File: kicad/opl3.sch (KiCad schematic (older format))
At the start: 44 parts, among them J1 Conn_01x08, J2 AudioJack2_Ground_Switch, U1 YMF262, U2 YAC512, U3 LM2902, U4 NE5532, U5 74HC595, U6 SN74LVC1G14DBV, X1 ASV-14.318MHz

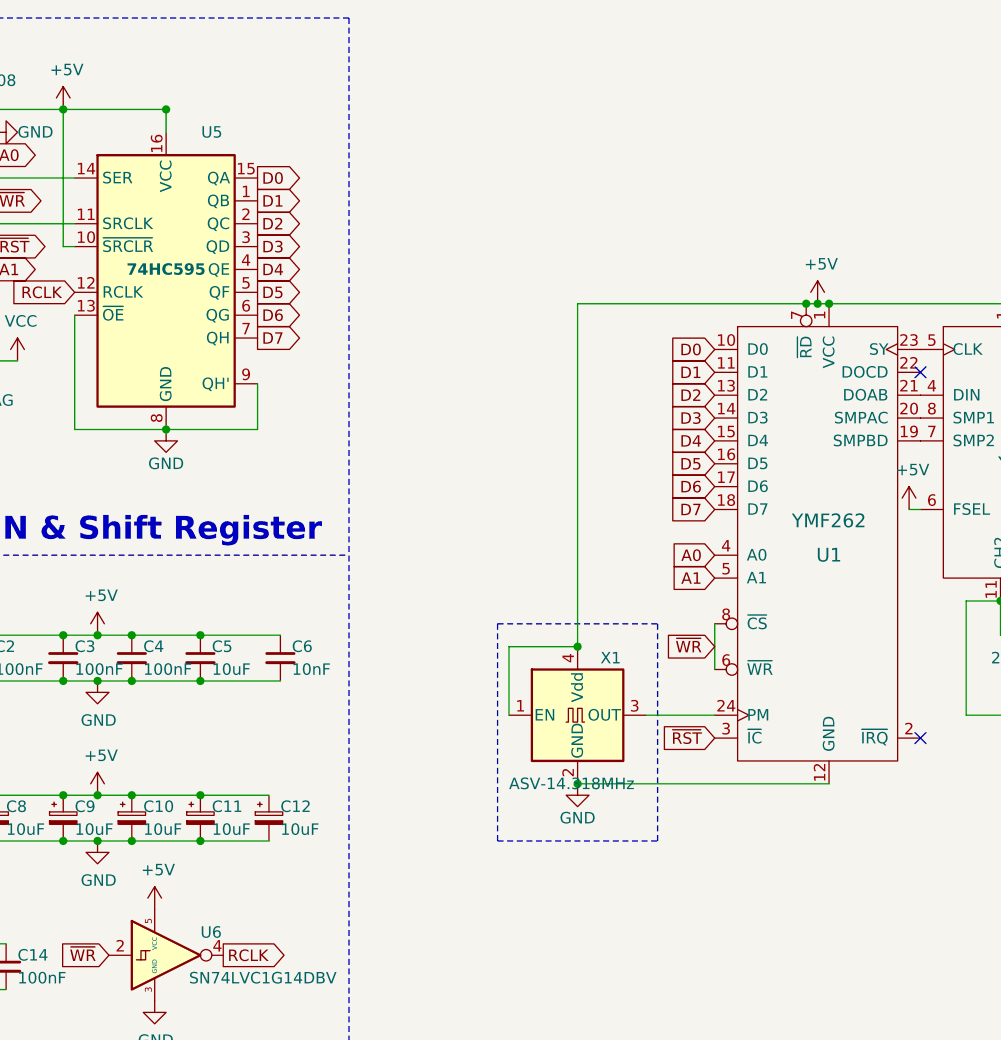
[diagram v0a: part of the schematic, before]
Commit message: A add on module enables ALL opl3's channel.
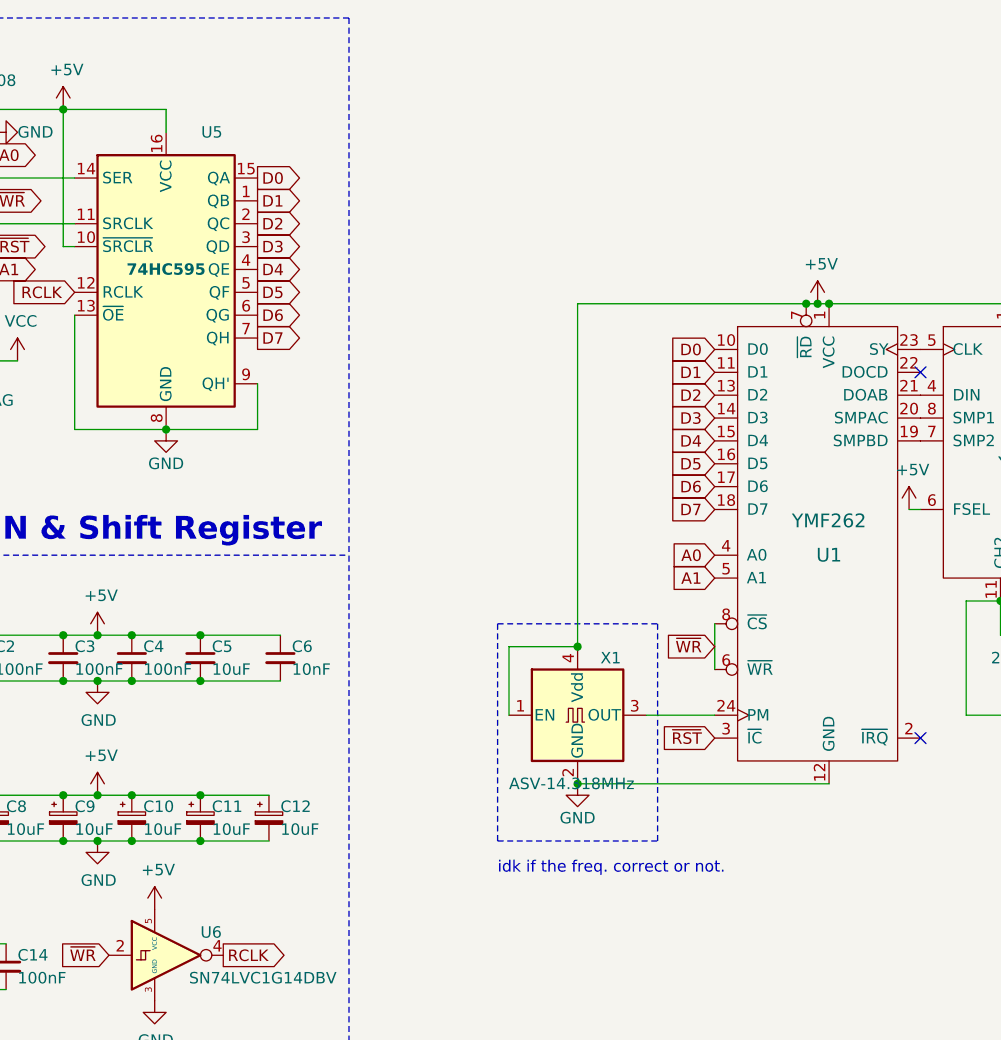
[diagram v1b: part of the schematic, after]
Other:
- note added: "idk if the freq. correct or not."
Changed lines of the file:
@@
 	-1   0    0    1
 $EndComp
-Connection ~ 2300 2150
 Connection ~ 1450 3250
 Wire Wire Line
 	1450 3250 1650 3250
+Text Notes 3750 5500 0    50   ~ 0
+idk if the freq. correct or not.
 $EndSCHEMATC
